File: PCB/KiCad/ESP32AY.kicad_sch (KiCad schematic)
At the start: 111 parts, among them J1 USB_C_Receptacle_USB2.0_14P, J2 MiniJack, J3 SD Card, Q1 BC807, Q2 BC817, Q3 BC817, SW1 Check bat, SW2 EN, SW3 BOOT, U1 AY-3-8910, U10 DS3231MZ, U11 MB85RC256V, U2 AY-3-8910, U3 CH340C, U4 ESP32-WROOM-32, U5 TPA6130A2RTJTG4, U6 IP5306, U7 AMS1117-3.3, U8 74HC595, U9 74HC595, Y3 12MHz

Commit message: Rev.C1 - initial PCM5102A DAC support
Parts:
- added C37, C39, C42, C43: 10uf, Capacitor_SMD:C_0805_2012Metric_Pad1.18x1.45mm_HandSolder, symbol Device:C_Small
- added C38, C40, C46: 100n, Capacitor_SMD:C_0805_2012Metric_Pad1.18x1.45mm_HandSolder, symbol Device:C_Small
- added C41: 2.2uf, Capacitor_SMD:C_0805_2012Metric_Pad1.18x1.45mm_HandSolder, symbol Device:C_Small
- added C44, C45: 2.2nf, Capacitor_SMD:C_0805_2012Metric_Pad1.18x1.45mm_HandSolder, symbol Device:C_Small
- added R43, R44: 10K, Resistor_SMD:R_0805_2012Metric_Pad1.20x1.40mm_HandSolder, symbol Device:R_Small
- added R45, R46: 1K, Resistor_SMD:R_0805_2012Metric_Pad1.20x1.40mm_HandSolder, symbol Device:R_Small
- added U12: PCM5102A, Package_SO:TSSOP-20_4.4x6.5mm_P0.65mm, symbol Audio:PCM5102A
- R18, R19, R32, R33: now not fitted; now left out of the parts list
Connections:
- net +3.3V: now also C46.1, U12.1 (CPVDD), U12.20 (DVDD), U12.8 (AVDD)
- net AYMIX_L: now also R46.1
- net AYMIX_R: now also R45.1
- net GND: now also C37.1, C38.1, C39.1, C40.1, C44.2, C45.2, C46.2, U12.10 (DEMP), U12.11 (FLT), U12.12 (SCK), U12.16 (FMT), U12.19 (DGND), U12.3 (CPGND), U12.9 (AGND)
- net DAC_SOUND_L renamed DAC_BCK
- net DAC_BCK: now also U12.13 (BCK)
- net DAC_SOUND_R renamed DAC_DAT
- net DAC_DAT: now also U12.14 (DIN)
- net USB_SENS renamed DAC_LRCK
- net DAC_LRCK: now also U12.15 (LRCK)
- new net: C42.2, R43.2
- new net: C41.1, U12.4 (CAPM)
- new net: C41.2, U12.2 (CAPP)
- new net: C39.2, C40.2, U12.18 (LDOO)
- new net: C37.2, C38.2, U12.5 (VNEG)
- new net: R43.1, U12.6 (OUTL)
- new net: R44.1, U12.7 (OUTR)
- new net: C43.2, R44.2
- new net PCM_L: C42.1, C44.1, R46.2
- new net PCM_R: C43.1, C45.1, R45.2
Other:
- note added: "* In case of using external DAC: - solder all the components described in this block - do not populate R18, R19, R32, R33"
- note added: "* In case of using internal DAC: - do not solder components described in this block - populate R18, R19, R32, R33"
- note added: "External DAC*"
- moved on the sheet: C15, C20, C32, C35, C36, C9, Encoder1, R13, R29, R31, R34, R35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

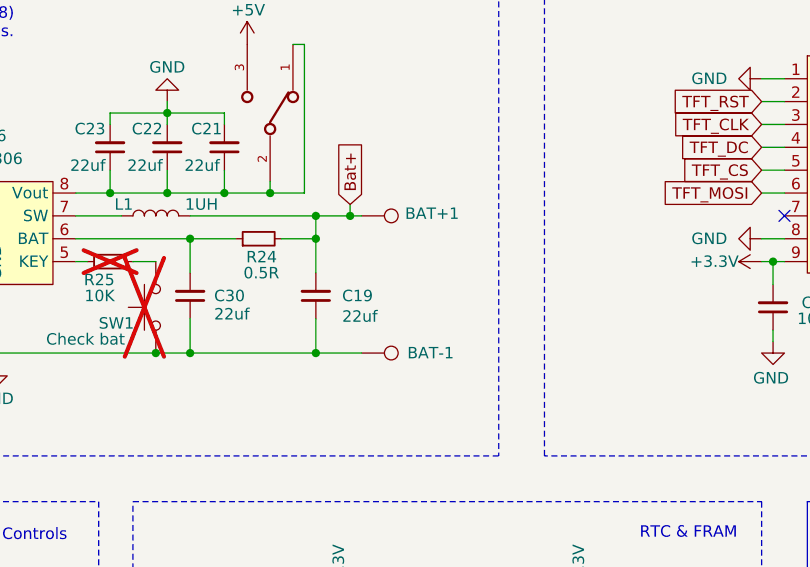
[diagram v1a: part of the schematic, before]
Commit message: Updated rev.C1 - added JST-PH connector
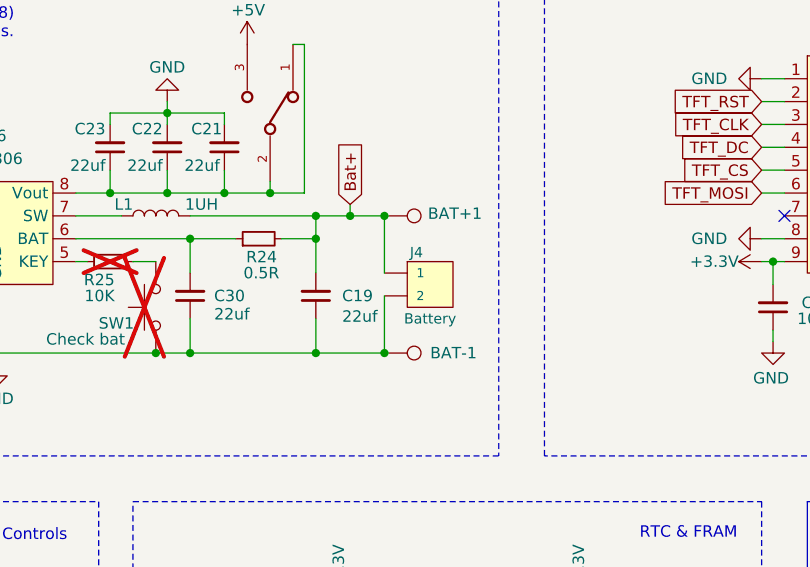
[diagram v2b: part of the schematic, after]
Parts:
- added J4: Battery, Connector_JST:JST_PH_S2B-PH-K_1x02_P2.00mm_Horizontal, symbol SparkFun-Connectors:CONN_02-JST-2MM-SMT
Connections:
- net Bat+: now also J4.1
- net GND: now also J4.2
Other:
- moved on the sheet: BAT+1, BAT-1
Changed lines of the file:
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@@
 	)
 	(junction
+		(at 161.29 168.91)
+		(diameter 0)
+		(color 0 0 0 0)
+	)
+	(junction
 		(at 25.4 201.93)
 		(diameter 0)
@@
 	)
 	(junction
+		(at 161.29 153.67)
+		(diameter 0)
+		(color 0 0 0 0)
+	)
+	(junction
 		(at 34.29 198.12)
 		(diameter 0)
@@
 	(wire
 		(pts
+			(xy 161.29 162.56) (xy 161.29 168.91)
+		)
+		(stroke
+			(width 0)
+			(type default)
+		)
+	)
+	(wire
+		(pts
 			(xy 33.02 45.72) (xy 35.56 45.72)
 		)
@@
 	(wire
 		(pts
-			(xy 158.75 168.91) (xy 153.67 168.91)
+			(xy 161.29 168.91) (xy 153.67 168.91)
 		)
 		(stroke
@@
 	(wire
 		(pts
+			(xy 161.29 153.67) (xy 161.29 160.02)
+		)
+		(stroke
+			(width 0)
+			(type default)
+		)
+	)
+	(wire
+		(pts
 			(xy 80.01 168.91) (xy 83.82 168.91)
 		)
@@
 	(wire
 		(pts
-			(xy 158.75 153.67) (xy 157.48 153.67)
+			(xy 161.29 153.67) (xy 157.48 153.67)
 		)
 		(stroke
@@
 	(symbol
 		(lib_id "Connector:TestPoint")
-		(at 158.75 168.91 270)
+		(at 161.29 168.91 270)
 		(unit 1)
 		(exclude_from_sim no)
@@
 		(dnp no)
 		(property "Reference" "BAT-1"
-			(at 163.83 168.91 90)
+			(at 166.37 168.91 90)
 			(effects
 				(font
@@
 		)
 		(property "Value" "BAT-"
-			(at 160.3498 170.307 0)
+			(at 162.8898 170.307 0)
 			(effects
 				(font
@@
 		)
 		(property "Footprint" "TestPoint:TestPoint_Pad_D3.0mm"
-			(at 158.75 173.99 0)
+			(at 161.29 173.99 0)
 			(effects
 				(font
@@
 		)
 		(property "Datasheet" "~"
-			(at 158.75 173.99 0)
+			(at 161.29 173.99 0)
 			(effects
 				(font
@@
 		)
 		(property "Description" ""
-			(at 158.75 168.91 0)
+			(at 161.29 168.91 0)
 			(effects
 				(font
@@
 	(symbol
 		(lib_id "Connector:TestPoint")
-		(at 158.75 153.67 270)
+		(at 161.29 153.67 270)
 		(unit 1)
 		(exclude_from_sim no)
@@
 		(dnp no)
 		(property "Reference" "BAT+1"
-			(at 163.576 153.416 90)
+			(at 166.116 153.416 90)
 			(effects
 				(font
@@
 		)
 		(property "Value" "BAT+"
-			(at 160.3498 155.067 0)
+			(at 162.8898 155.067 0)
 			(effects
 				(font
@@
 		)
 		(property "Footprint" "TestPoint:TestPoint_Pad_D3.0mm"
-			(at 158.75 158.75 0)
+			(at 161.29 158.75 0)
 			(effects
 				(font
@@
 		)
 		(property "Datasheet" "~"
-			(at 158.75 158.75 0)
+			(at 161.29 158.75 0)
 			(effects
 				(font
@@
 		)
 		(property "Description" ""
-			(at 158.75 153.67 0)
+			(at 161.29 153.67 0)
 			(effects
 				(font
@@
 					(unit 1)
 				)
+			)
+		)
+	)
+	(symbol
+		(lib_id "SparkFun-Connectors:CONN_02-JST-2MM-SMT")
+		(at 163.83 160.02 180)
+		(unit 1)
+		(exclude_from_sim no)
+		(in_bom yes)
+		(on_board yes)
+		(dnp no)
+		(property "Reference" "J4"
+			(at 164.846 157.734 0)
+			(effects
+				(font
+					(size 1.143 1.143)
+				)
+			)
+		)
+		(property "Value" "Battery"
+			(at 166.37 165.1 0)
+			(effects
+				(font
+					(size 1.143 1.143)
+				)
+			)
+		)
+		(property "Footprint" "Connector_JST:JST_PH_S2B-PH-K_1x02_P2.00mm_Horizontal"
+			(at 163.83 167.64 0)
+			(effects
+				(font
+					(size 0.508 0.508)
+				)
+				(hide yes)
+			)
+		)
+		(property "Datasheet" ""
+			(at 163.83 160.02 0)
+			(effects
+				(font
+					(size 1.27 1.27)
+				)
+				(hide yes)
+			)
+		)
+		(property "Description" "Multi connection point. Often used as Generic Header-pin footprint for 0.1 inch spaced/style header connections  <b>On any of the 0.1 inch spaced packages, you can populate with these:</b><ul><li><a href=\"https://www.sparkfun.com/products/116\"> Break Away Headers - Straight</a> (PRT-00116)</li><li><a href=\"https://www.sparkfun.com/products/553\"> Break Away Male Headers - Right Angle</a> (PRT-00553)</li><li><a href=\"https://www.sparkfun.com/products/115\"> Female Headers</a> (PRT-00115)</li><li><a href=\"https://www.sparkfun.com/products/117\"> Break Away Headers - Machine Pin</a> (PRT-00117)</li><li><a href=\"https://www.sparkfun.com/products/743\"> Break Away Female Headers - Swiss Machine Pin</a> (PRT-00743)</li></ul> <b> For SCREWTERMINALS and SPRING TERMINALS visit here:</b><ul><li><a href=\"https://www.sparkfun.com/search/results?term=Screw+Terminals\"> Screw Terimnals on SparkFun.com</a> (5mm/3.5mm/2.54mm spacing)</li></ul> <b>This device is also useful as a general connection point to wire up your design to another part of your project. Our various solder wires solder well into these plated through hole pads.</b><ul><li><a href=\"https://www.sparkfun.com/products/11375\"> Hook-Up Wire - Assortment (Stranded, 22 AWG)</a> (PRT-11375)</li><li><a href=\"https://www.sparkfun.com/products/11367\"> Hook-Up Wire - Assortment (Solid Core, 22 AWG)</a> (PRT-11367)</li><li><a href=\"https://www.sparkfun.com/categories/141\"> View the entire wire category on our website here</a></li> </ul> <b>Special notes:</b> Molex polarized connector foot print use with: PRT-08233 with associated crimp pins and housings.<br><br>2.54_SCREWTERM for use with  PRT-10571.<br><br>3.5mm Screw Terminal footprints for  PRT-08084<br><br>5mm Screw Terminal footprints for use with PRT-08432"
+			(at 163.83 160.02 0)
+			(effects
+				(font
+					(size 1.27 1.27)
+				)
+				(hide yes)
+			)
+		)
+		(property "Field5" "CONN-11443"
+			(at 166.37 166.37 0)
+			(effects
+				(font
+					(size 1.524 1.524)
+				)
+				(hide yes)
+			)
+		)
+		(pin "2"
+		)
+		(pin "1"
+		)
+		(instances
+			(project ""
+				(path "/425f36ea-ae27-435f-aa55-f13e69cbacb6"
+					(reference "J4")
+					(unit 1)
+				)

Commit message: Rev.C2 initial revision
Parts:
- removed C21, C22, C23, C30: 22uf, Capacitor_SMD:C_1206_3216Metric_Pad1.33x1.80mm_HandSolder, symbol Device:C_Small
- removed D3: 75%, LED_SMD:LED_0805_2012Metric, symbol Device:LED
- removed R24: 0.5R, Resistor_SMD:R_0805_2012Metric, symbol Device:R_Small
- removed R25: 10K, Resistor_SMD:R_0805_2012Metric, symbol Device:R_Small
- removed SW1: Check bat, Jumper:SolderJumper-2_P1.3mm_Open_RoundedPad1.0x1.5mm, symbol Switch:SW_Push
- removed U6: IP5306, Package_SO:HSOP-8-1EP_3.9x4.9mm_P1.27mm_EP2.41x3.1mm, symbol Module:SM5308
- added C14, C17: 22uf, Capacitor_SMD:C_1206_3216Metric_Pad1.33x1.80mm_HandSolder, symbol Device:C_Small
- added D3: SS14, Diode_SMD:D_SMA, symbol Diode:SS14
- added R10, R21: 1k, Resistor_SMD:R_0805_2012Metric_Pad1.20x1.40mm_HandSolder, symbol Device:R_Small
- added R16: 2k*, Resistor_SMD:R_0805_2012Metric_Pad1.20x1.40mm_HandSolder, symbol Device:R_Small
- added R19: 47k, Resistor_SMD:R_0805_2012Metric_Pad1.20x1.40mm_HandSolder, symbol Device:R_Small
- added R20: 6.2k, Resistor_SMD:R_0805_2012Metric_Pad1.20x1.40mm_HandSolder, symbol Device:R_Small
- added U4: TP4056, Package_SO:SOIC-8-1EP_3.9x4.9mm_P1.27mm_EP2.41x3.3mm_ThermalVias, symbol Battery_Management:TP4056-42-ESOP8
- added U7: SDB628, Package_TO_SOT_SMD:SOT-23-6_Handsoldering, symbol retro:SDB628
- BAT+1: value BAT+ -> +
- BAT-1: value BAT- -> -
- D1: value 25% -> OK
- D2: value 50% -> CHRG
- D4: value 100% -> PWR
- L1: value 1UH -> 22uH; footprint Inductor_SMD:L_7.3x7.3_H3.5 -> Inductor_SMD:L_Bourns_SRN8040TA
- renumbered C4 to C1, C18 to C10, C19 to C11, C2 to C12, C28 to C13, C36 to C15, C35 to C16, C1 to C18, C31 to C19, C3 to C2, C29 to C20, C46 to C21, C27 to C22, C41 to C23, C37 to C24, C38 to C25, C42 to C26, C44 to C27, C43 to C28, C39 to C29, C16 to C3, C45 to C30, C40 to C31, C11 to C32, C12 to C33, C13 to C34, C14 to C35, C33 to C36, C34 to C37, C10 to C38, C5 to C39, C26 to C4, C15 to C40, C9 to C41, C8 to C42, C7 to C43, C6 to C44, C24 to C5, C20 to C6, C32 to C7, C25 to C8, C17 to C9, J4 to J2, J2 to J4, R40 to R1, R38 to R11, R19 to R12, R18 to R13, R6 to R14, R7 to R15, R31 to R17, R29 to R18, R39 to R2, R20 to R22, R3 to R23, R28 to R24, R30 to R25, R43 to R26, R44 to R27, R1 to R28, R21 to R29, R41 to R3, R22 to R30, R2 to R31, R4 to R32, R5 to R33, R12 to R34, R9 to R35, R17 to R36, R14 to R37, R33 to R38, R32 to R39, R42 to R4, R11 to R40, R10 to R41, R16 to R42, R15 to R43, R26 to R44, R27 to R45, R13 to R46, R8 to R47, R45 to R48, R46 to R49, R23 to R5, R34 to R6, R35 to R7, R37 to R8, R36 to R9, S2 to S1, S4 to S2, S6 to S3, SW3 to SW1, U7 to U1, U12 to U10, U4 to U11, U3 to U12, U5 to U13, U8 to U2, U9 to U3, U1 to U5, U10 to U6, U2 to U8, U11 to U9, Y3 to Y1
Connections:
- net +5V: now also C17.2, D3.1 (K), R19.1, R21.1; no longer S3.3
- net Bat+: now also S3.1, S3.2, U4.5 (BAT); no longer L1.2
- net GND: now also D4.1 (K), C14.1, C17.1, R16.2, R20.2, U4.1 (TEMP), U4.3 (GND), U4.9 (EPAD), U7.2 (GND)
- net Vin: now also R10.1, U4.4 (V_{CC}), U4.8 (CE)
- net STPUP_VIN: now reaches L1.1
- net STPUP_VIN: now also S3.3, C14.2, U7.4 (EN), U7.5 (VIN)
- net at D2.1 (K): now also U4.7 (~{CHRG}); no longer D1.2 (A)
- new net: D3.2 (A), L1.2, U7.1 (SW)
- new net: D4.2 (A), R21.2
- new net: R16.1, U4.2 (PROG)
- new net: D1.1 (K), U4.6 (~{STDBY})
- new net: R19.2, R20.1, U7.3 (FB)
- new net: D1.2 (A), D2.2 (A), R10.2
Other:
- note added: "* In case of using external DAC: - solder all the components described in this block - do not populate R38, R39, R12, R13"
- note added: "* In case of using internal DAC: - do not solder components described in this block - populate R38, R39, R12, R13"
- note added: "Please note: in case of using CH340G please populate Y1, C36, C37"
- note added: "R16 value should be adjusted to limit the charging current: 2k is for ~500mA"
- note added: "RTC & EEPROM"
- note added: "USB Charger and step-up"
- note removed: "* In case of using external DAC: - solder all the components described in this block - do not populate R18, R19, R32, R33"
- note removed: "* In case of using internal DAC: - do not solder components described in this block - populate R18, R19, R32, R33"
- note removed: "Please make sure to use exactly the same IP5306 IC. Other ICs (like FM5324, SM5308) has some issues with sleep/wakeup modes."
- note removed: "Please note: in case of using CH340G please populate Y3, C33, C34"
- note removed: "RTC & FRAM"
- note removed: "USB Charger and step-up SoC"
- moved on the sheet: BAT+1, BAT-1, C10, C11, C19, C9, D1, D2, D4, J1, J2, Q1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
